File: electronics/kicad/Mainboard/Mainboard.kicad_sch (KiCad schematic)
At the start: 26 parts, among them J1 MCU Power, J10 Box Button 1, J11 Box Button 2, J12 Conn_01x05, J13 Extra Button, J2 Conn_01x05, J3 Conn_01x05, J4 Conn_01x05, J5 Conn_01x05, J6 Conn_01x05, J7 X-Axis Hall, J8 Y-Axis Hall, J9 USB_A_Stacked, U1 ESP32-C6-DevKitC-1, U2 MCP23017_SP, U3 SP3485CP

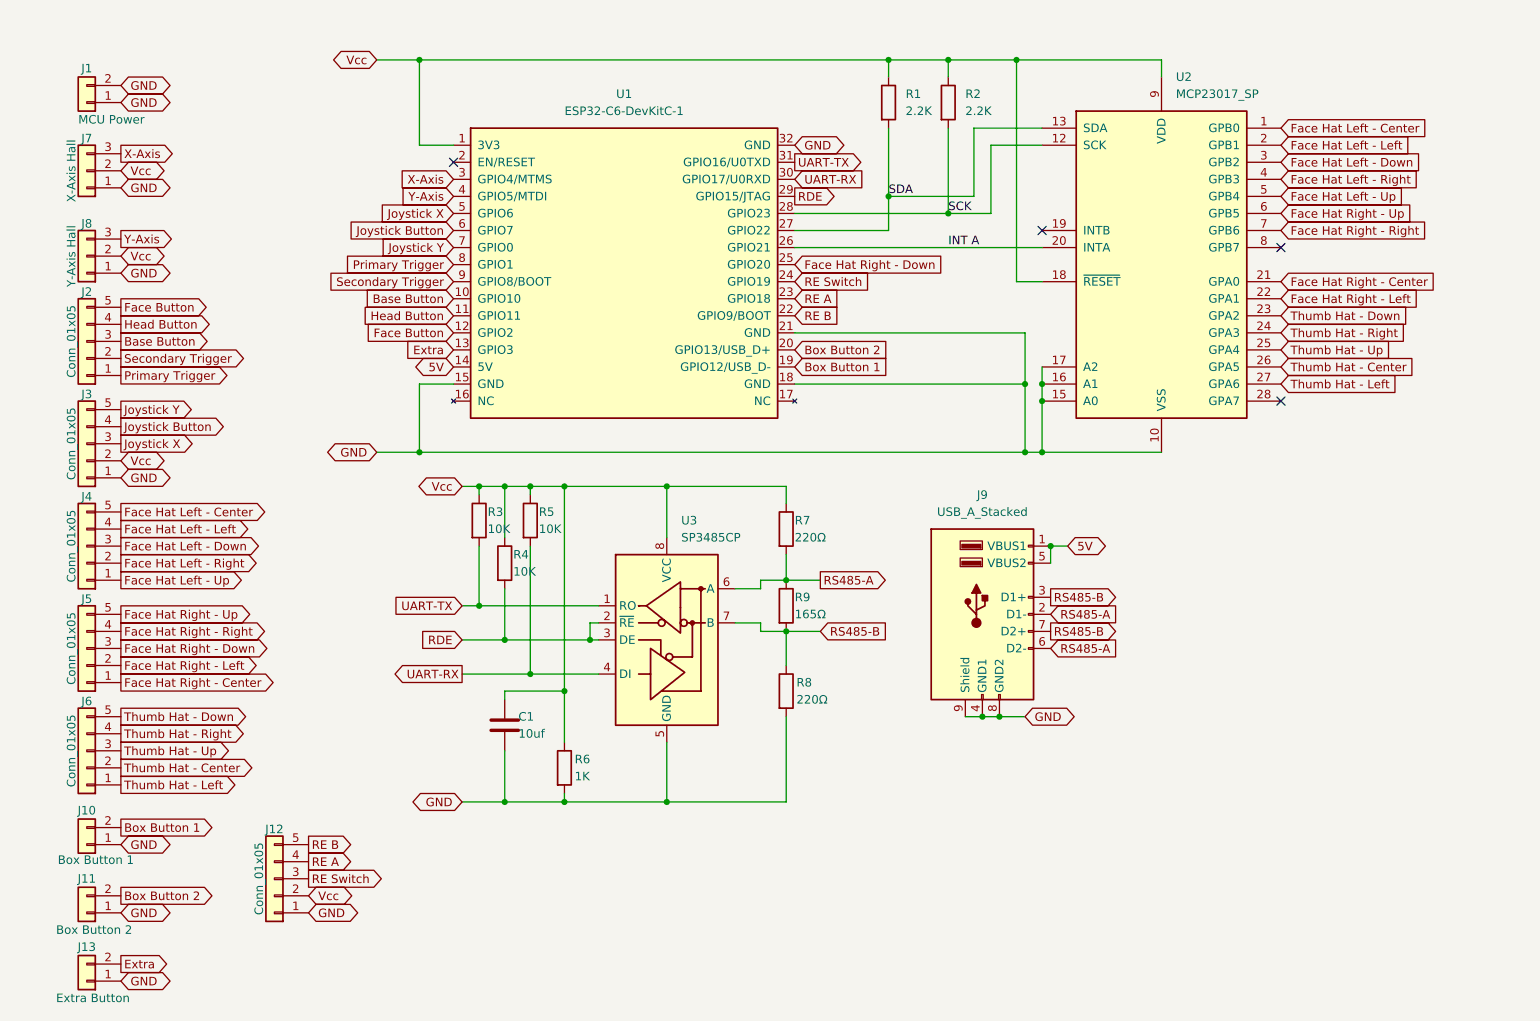
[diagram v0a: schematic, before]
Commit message: Updated PCB with New Silkscreen
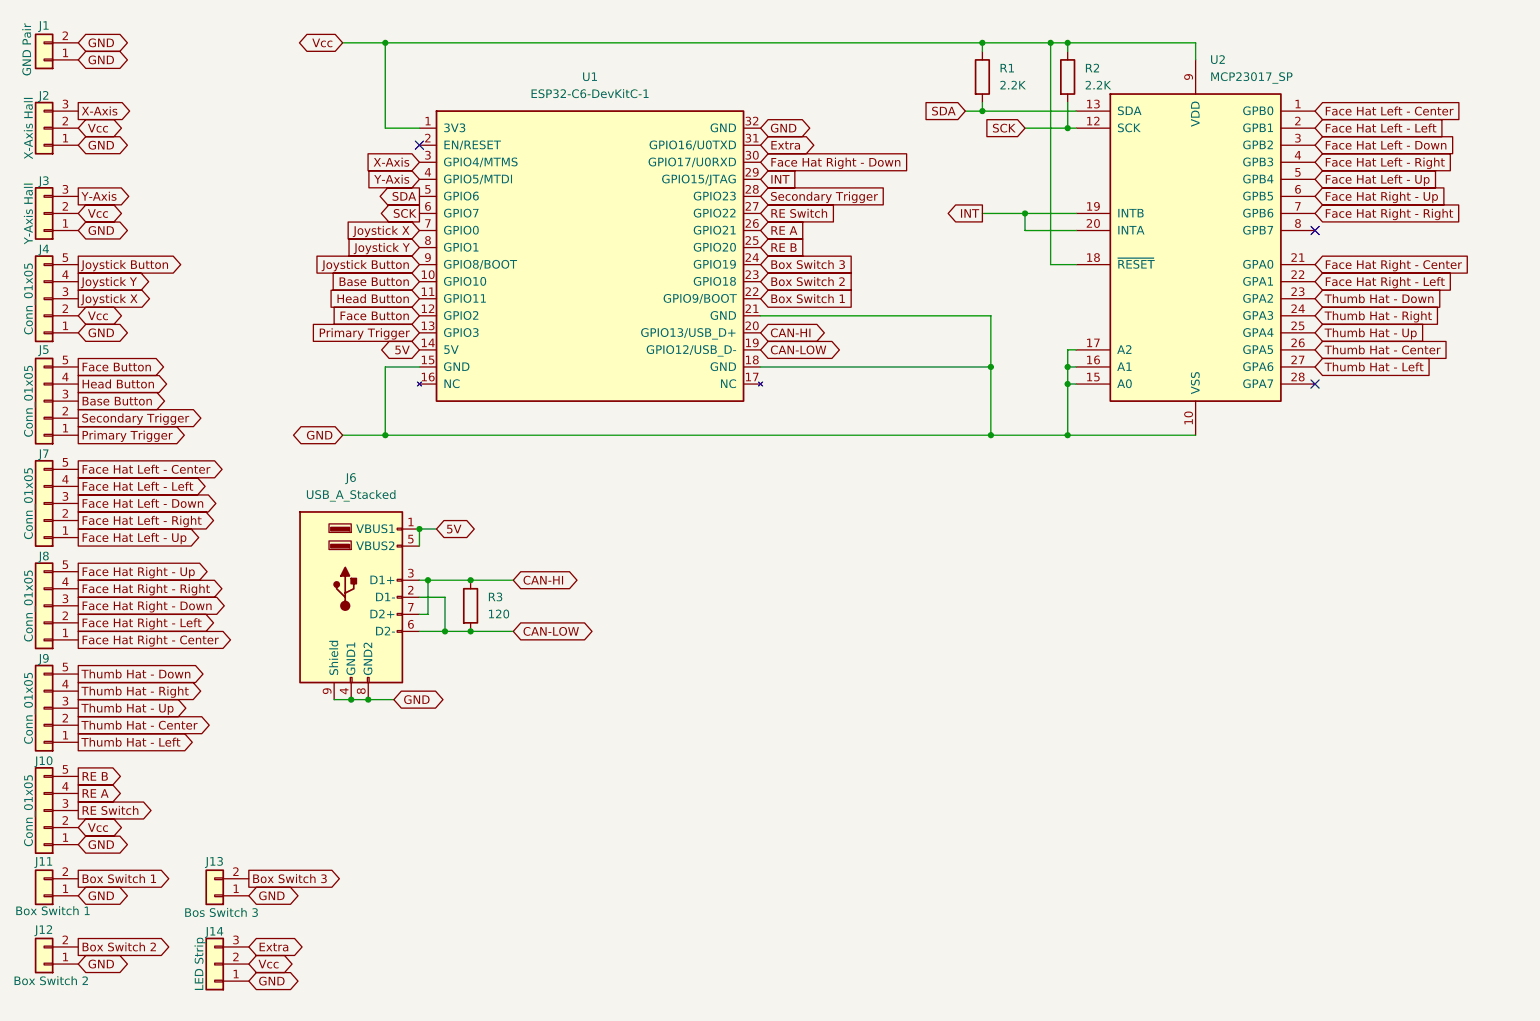
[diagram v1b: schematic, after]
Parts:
- removed C1: 10uf, Capacitor_THT:CP_Radial_D4.0mm_P2.00mm, symbol Device:C
- removed R4, R5: 10K, Resistor_THT:R_Axial_DIN0204_L3.6mm_D1.6mm_P5.08mm_Horizontal, symbol Device:R
- removed R6: 1K, Resistor_THT:R_Axial_DIN0204_L3.6mm_D1.6mm_P5.08mm_Horizontal, symbol Device:R
- removed R7, R8: 220Ω, Resistor_THT:R_Axial_DIN0204_L3.6mm_D1.6mm_P5.08mm_Horizontal, symbol Device:R
- removed R9: 165Ω, Resistor_THT:R_Axial_DIN0204_L3.6mm_D1.6mm_P5.08mm_Horizontal, symbol Device:R
- removed U3: SP3485CP, Package_DIP:DIP-8_W7.62mm, symbol Interface_UART:SP3485CP
- added J14: LED Strip, Connector_JST:JST_PH_B3B-PH-K_1x03_P2.00mm_Vertical, symbol Connector_Generic:Conn_01x03
- J1: value MCU Power -> GND Pair
- J11: renamed from J10; value Box Button 1 -> Box Switch 1
- J12: renamed from J11; value Box Button 2 -> Box Switch 2
- J13: value Extra Button -> Bos Switch 3
- R3: value 10K -> 120
- renumbered J12 to J10, J7 to J2, J8 to J3, J3 to J4, J2 to J5, J9 to J6, J4 to J7, J5 to J8, J6 to J9
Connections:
- net RDE is gone; now on net INT: U1.29 (GPIO15/JTAG)
- net UART-RX is gone; now on net Face Hat Right - Down: U1.30 (GPIO17/U0RXD)
- net Extra: now also U1.31 (GPIO16/U0TXD), J14.3 (Pin_3); no longer J13.2 (Pin_2), U1.13 (GPIO3)
- net Face Hat Right - Down: no longer U1.25 (GPIO20)
- net GND: now also J14.1 (Pin_1)
- net Joystick Button: now also J4.5 (Pin_5), U1.9 (GPIO8/BOOT); no longer J4.4 (Pin_4), U1.6 (GPIO7)
- net Joystick X: now also U1.7 (GPIO0); no longer U1.5 (GPIO6)
- net Joystick Y: now also J4.4 (Pin_4), U1.8 (GPIO1); no longer J4.5 (Pin_5), U1.7 (GPIO0)
- net Primary Trigger: now also U1.13 (GPIO3); no longer U1.8 (GPIO1)
- net RE A: now also U1.26 (GPIO21); no longer U1.23 (GPIO18)
- net RE B: now also U1.25 (GPIO20); no longer U1.22 (GPIO9/BOOT)
- net RE Switch: now also U1.27 (GPIO22); no longer U1.24 (GPIO19)
- net SCK: now also U1.6 (GPIO7); no longer U1.28 (GPIO23)
- net SDA: now also U1.5 (GPIO6); no longer U1.27 (GPIO22)
- net Secondary Trigger: now also U1.28 (GPIO23); no longer U1.9 (GPIO8/BOOT)
- net Vcc: now also J14.2 (Pin_2); no longer R3.1
- net INT: now reaches U2.19 (INTB)
- net INT: now also U2.20 (INTA)
- net Box Button 1 renamed Box Switch 1
- net Box Switch 1: now also U1.22 (GPIO9/BOOT); no longer U1.19 (GPIO12/USB_D-)
- net Box Button 2 renamed Box Switch 2
- net Box Switch 2: now also U1.23 (GPIO18); no longer U1.20 (GPIO13/USB_D+)
- removed net INT A: U1.26 (GPIO21), U2.20 (INTA)
- net RS485-A renamed CAN-LOW
- net CAN-LOW: now also R3.2, U1.19 (GPIO12/USB_D-)
- net RS485-B renamed CAN-HI
- net CAN-HI: now also R3.1, U1.20 (GPIO13/USB_D+)
- removed net UART-TX: R3.2, U1.31 (GPIO16/U0TXD)
- new net Box Switch 3: J13.2 (Pin_2), U1.24 (GPIO19)
- no-connect marks 4 -> 3
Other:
- moved on the sheet: J1, J10, J11, J12, J13, J2, J3, J4, J5, J6, J7, J8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
